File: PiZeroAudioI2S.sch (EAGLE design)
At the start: 53 parts, among them CN1 1X4-BIG, CON1 RPI-ZERO, J1 1X2-3.5MM, U3 NC7WZ16, U4 TPA3144D2PWPR

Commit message: Added I2C and Amplifier
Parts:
- removed C1, C11, C2, C26, C4, C5: 100nF, adafruit:C-USC0805
- removed C10, C15, C16, C20, C22, C25: 1nF, resistor:C-EUC0805
- removed C12: 100uF, adafruit:C-USC0805
- removed C13, C17, C18, C23: 220nF, resistor:C-EUC0805
- removed C14, C19, C21, C24: 1uF, resistor:C-EUC0805
- removed C27: 100UF, adafruit:C-USC0805
- removed CON1: RPI-ZERO, RPI-Zero:RPI-ZERO
- removed L1, L2, L3, L4: BLM31A, HappyBrackets:BLM31A
- removed R10: 39K, adafruit:R-US_R0805
- removed R11: 56K, adafruit:R-US_R0805
- removed R12, R13, R14: 33K, adafruit:R-US_R0805
- removed R15: 10R, adafruit:R-US_R0805
- removed R3, R6: 220, adafruit:R-US_R0805
- removed R4: 100, adafruit:R-US_R0805
- removed R5: 1K8, adafruit:R-US_R0805
- removed R9: 10K, adafruit:R-US_R0805
- removed U1: (no value), adafruit:TXB0104PWR
- removed U3: NC7WZ16, fairchild:NC7WZ16
- removed U4: TPA3144D2PWPR, HappyBrackets:TPA3144D2PWPR
- added U$1: RPI-ZERO, RPI-Zero:RPI-ZERO
- added U$2: (no value), HappyBrackets:LSM6DS33LGA-16-3X3
- added U$3: PCM5100A, HappyBrackets:PCM5100A
- C7: value 47uF -> 100nF; device adafruit:CPOL-US085CS-1AR -> adafruit:C-USC0805
- R1: value 10K -> 220
- R2: value 10K -> 100
- R7: value 100 -> 10K
- R8: value 1K8 -> 10K
- U2: device HappyBrackets:LSM6DS33LGA-16-3X3 -> adafruit:TXB0104PWR
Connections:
- removed net /MUTE: R9.1
- removed net AUDIO-R: C7.-, R8.2, U4.RINP-12
- removed net N$10: C23.2, U4.17-BSPR
- removed net N$11: C16.2, CN1.2, L2.2
- removed net N$12: C15.1, CN1.1, L1.2
- removed net N$13: C18.2, U4.21-BSNR
- removed net N$14: C20.1, CN1.3, L3.2
- removed net N$15: C22.2, CN1.4, L4.2
- removed net N$16: C17.2, U4.22-BSNL
- removed net N$17: C13.2, U4.26-BSPL
- removed net N$18: C13.1, L1.1, U4.25-OUTPL
- removed net N$19: C17.1, L2.1, U4.23-OUTNL
- removed net N$2: R3.2, U3.Y1
- removed net N$20: C18.1, L3.1, U4.20-OUTNR
- removed net N$21: C23.1, L4.1, U4.18-OUTPR
- removed net N$23: R12.1, R13.2, U4.GAIN-6
- removed net N$24: R13.1, R14.2, U4.SSCTRL-7
- removed net N$25: R10.1, R11.2, U4.LIMTHRES-8
- removed net N$26: C19.1, R11.1, R14.1, U4.GVDD-9, U4.LIMRATE-5
- removed net N$3: R6.2, U3.Y2
- removed net N$4: C7.+, C9.1, R6.1, R7.2
- removed net N$5: R9.2, U4./FAULT-2, U4./SD-1
- removed net N$6: U4.LINP-3
- removed net N$7: C14.1, U4.LINN-4
- removed net N$8: C21.1, U4.RINN-11
- removed net N$9: C24.1, R15.1, U4.AVCC-14
- new net OUTL+: CN1.2
- new net OUTL-: CN1.1
- new net OUTR+: CN1.3
- new net OUTR-: CN1.4
- net +3V3: now also C7.1, R7.1, R8.1, U$1.3V3@1, U$2.CS, U$2.SDO, U$2.VDD, U$2.VDDIO, U2.VCCA; no longer C1.1, C5.1, CON1.3V3@1, R1.1, R2.1, U1.VCCA, U2.CS, U2.SDO, U2.VDD, U2.VDDIO, U3.VCC
- net +5V: now also C9.1, U$1.5V0@1, U$1.5V0@2, U2.VCCB; no longer C10.1, C11.1, C12.1, C2.1, C25.1, C26.1, C27.1, CON1.5V0@1, CON1.5V0@2, R15.2, U1.VCCB, U4.15-PVCC, U4.16-PVCC, U4.27-PVCC, U4.28-PVCC
- net AUDIO-L: no longer R5.2
- net GND: now also C7.2, U$1.GND@1, U$1.GND@2, U$1.GND@3, U$1.GND@4, U$1.GND@5, U$1.GND@6, U$1.GND@7, U$1.GND@8, U$2.GND, U$2.GND2, U$2.RES1, U$2.RES2, U$2.RES3, U$2.RES4, U$2.RES5; no longer C1.2, C10.2, C11.2, C12.2, C14.2, C15.2, C16.1, C19.2, C2.2, C20.2, C21.2, C22.1, C24.2, C25.2, C26.2, C27.2, C4.2, C5.2, CON1.GND@1, CON1.GND@2, CON1.GND@3, CON1.GND@4, CON1.GND@5, CON1.GND@6, CON1.GND@7, CON1.GND@8, R10.2, R12.2, R4.1, R5.1, R7.1, R8.1, U1.GND, U2.GND2, U2.RES1, U2.RES2, U2.RES3, U2.RES4, U2.RES5, U3.GND, U4.19-GND, U4.1SPW-13, U4.24-GND, U4.GND-10
- net N$1: now also R1.1; no longer C4.1, R3.1, R4.2
- net PWM-LEFT: now also U$1.GPIO18; no longer CON1.GPIO18, U3.A1
- net PWM-RIGHT: now also U$1.GPIO13; no longer CON1.GPIO13, U3.A2
- net SCL: now also R8.2, U$1.GPIO3/SCL1, U$2.SCL; no longer CON1.GPIO3/SCL1, R2.2, U2.SCL
- net SDA: now also R7.2, U$1.GPIO2/SDA1, U$2.SDA; no longer CON1.GPIO2/SDA1, R1.2, U2.SDA
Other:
- note removed: "Accel + Gyro"
- note removed: "GPIO"
- note removed: "PCM Audio"
- note removed: "PWR amp"
- note removed: "RPI Header"
- note removed: "To Speakers"
- moved on the sheet: C3, C6, C8, C9, CN1, R1, R2, R7, R8

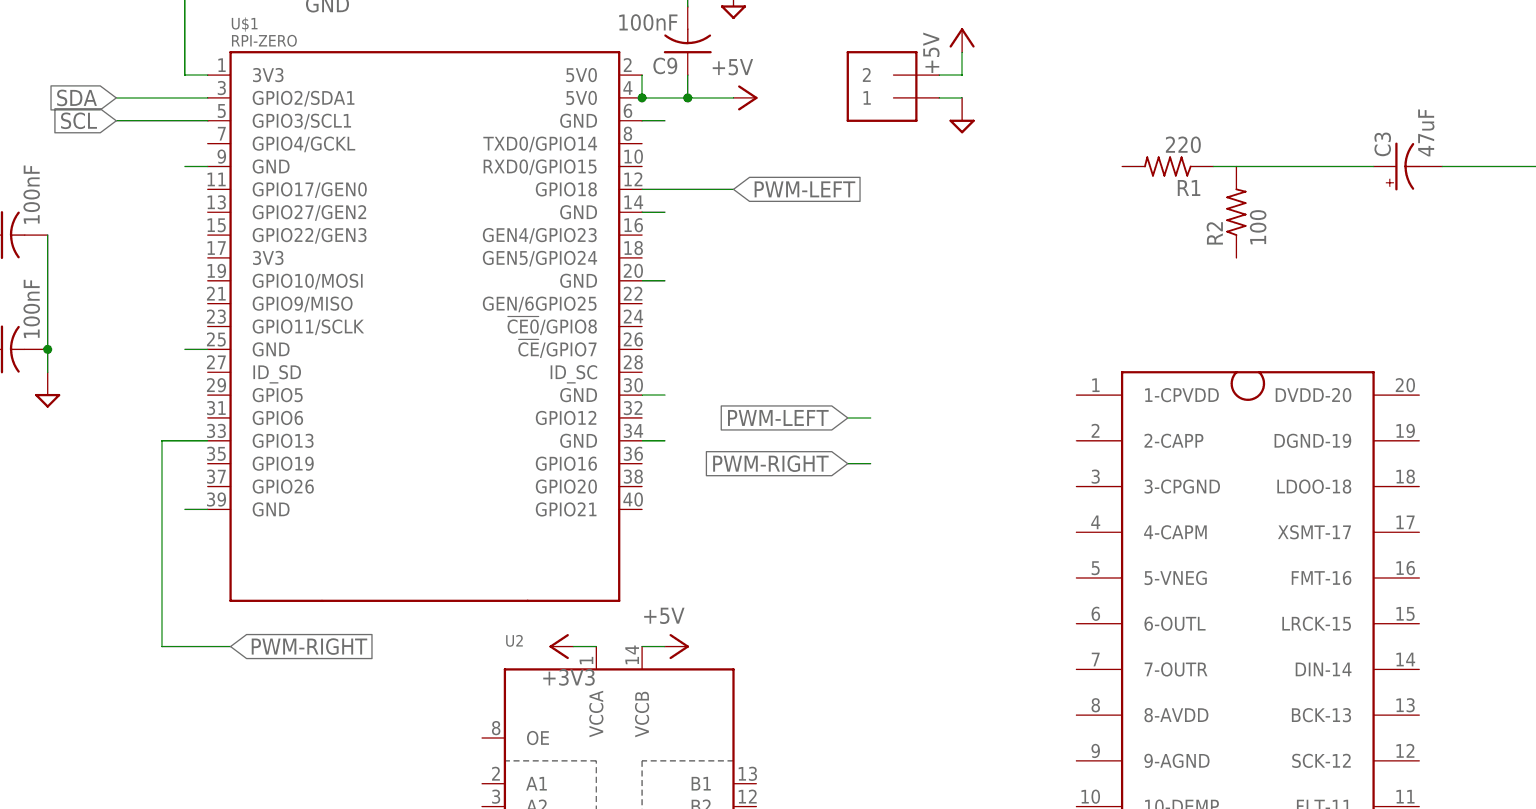
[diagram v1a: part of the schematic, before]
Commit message: Renumbered Pins Placed components for first board
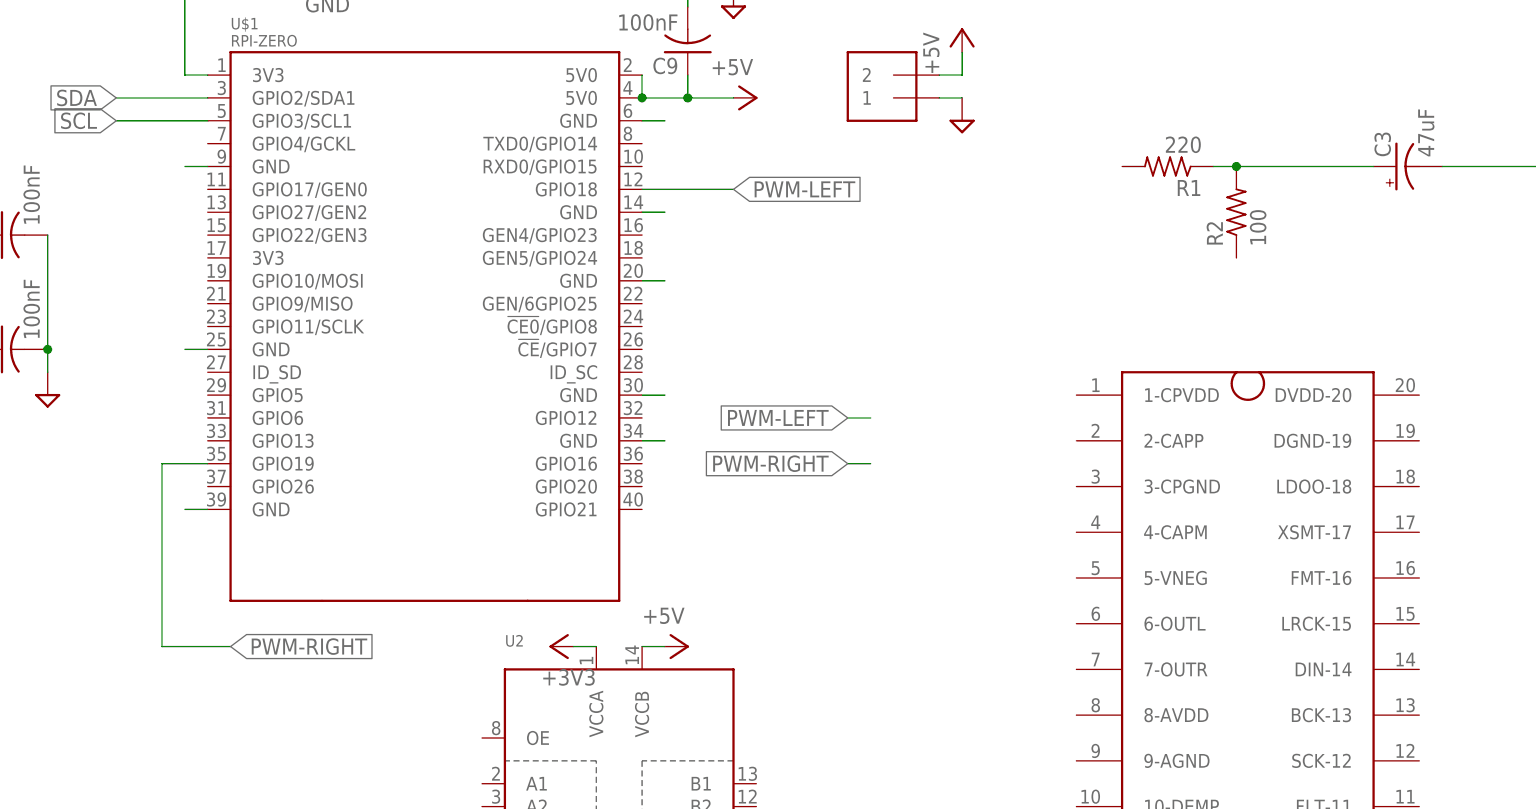
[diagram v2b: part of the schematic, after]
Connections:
- net N$1: now also R2.2
- net PWM-RIGHT: now also U$1.GPIO19; no longer U$1.GPIO13
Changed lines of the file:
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@@
 <net name="PWM-RIGHT" class="0">
 <segment>
-<pinref part="U$1" gate="G$1" pin="GPIO13"/>
-<wire x1="-228.6" y1="88.9" x2="-233.68" y2="88.9" width="0.1524" layer="91"/>
-<wire x1="-233.68" y1="88.9" x2="-233.68" y2="66.04" width="0.1524" layer="91"/>
 <wire x1="-233.68" y1="66.04" x2="-226.06" y2="66.04" width="0.1524" layer="91"/>
 <label x="-226.06" y="66.04" size="1.778" layer="95" xref="yes"/>
+<pinref part="U$1" gate="G$1" pin="GPIO19"/>
+<wire x1="-228.6" y1="86.36" x2="-233.68" y2="86.36" width="0.1524" layer="91"/>
+<wire x1="-233.68" y1="86.36" x2="-233.68" y2="66.04" width="0.1524" layer="91"/>
 </segment>
 <segment>
@@
 <segment>
 <pinref part="R1" gate="G$1" pin="1"/>
-<wire x1="-116.84" y1="119.38" x2="-99.06" y2="119.38" width="0.1524" layer="91"/>
+<wire x1="-116.84" y1="119.38" x2="-114.3" y2="119.38" width="0.1524" layer="91"/>
 <pinref part="C3" gate="G$1" pin="+"/>
+<pinref part="R2" gate="G$1" pin="2"/>
+<wire x1="-114.3" y1="119.38" x2="-99.06" y2="119.38" width="0.1524" layer="91"/>
+<junction x="-114.3" y="119.38"/>
 </segment>
 </net>

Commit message: Pre- grove connector
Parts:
- removed C3: 47uF, adafruit:CPOL-US085CS-1AR
- removed C6, C7, C8: 100nF, adafruit:C-USC0805
- removed R7, R8: 10K, adafruit:R-US_R0805
- removed U$1: RPI-ZERO, RPI-Zero:RPI-ZERO
- removed U$2: (no value), HappyBrackets:LSM6DS33LGA-16-3X3
- removed U$3: PCM5100A, HappyBrackets:PCM5100A
- added C1, C10, C2, C25, C5: 100nF, rcl:C-EUC0603
- added C11: 100uF, adafruit:CPOL-USCT3528
- added C12, C16, C17, C22: 220nF, rcl:C-EUC0603
- added C13, C18, C20, C23: 1uF, rcl:C-EUC0603
- added C14, C15, C19, C21, C24: 1nF, rcl:C-EUC0603
- added C26: 100UF, adafruit:CPOL-USCT3528
- added CON1: RPI-ZERO, RPI-Zero:RPI-ZERO
- added JP1: GPIO, adafruit:PINHD-2X4
- added JP2: (no value), adafruit:PINHD-1X3
- added L1, L2, L3, L4: FB, HappyBrackets:NFZ2MSML0806
- added LED1: (no value), adafruit:LEDCHIP-LED0805
- added Q1: DMG2305UX, HappyBrackets:DMG2305UX
- added R10: 39K, adafruit:R-US_R0603
- added R11: 56K, adafruit:R-US_R0603
- added R12, R13, R14: 33K, adafruit:R-US_R0603
- added R15: 10R, adafruit:R-US_R0603
- added R16, R17: 220, adafruit:R-US_R0603
- added R3: 47K, adafruit:R-US_R0603
- added R4, R9: 10K, adafruit:R-US_R0603
- added SH1, SH2: SHORT, HappyBrackets:SHORT
- added U1: TXB0104PWR, adafruit:TXB0104PWR
- added U3: PCM5101A, HappyBrackets:PCM5101A
- added U4: TPA3144D2PWPR, HappyBrackets:TPA3144D2PWPR
- added U5: DMMT5401, HappyBrackets:DMMT5401
- C9: value 100nF -> 1nF; device adafruit:C-USC0805 -> rcl:C-EUC0603
- R1: value 220 -> 10K; device adafruit:R-US_R0805 -> adafruit:R-US_R0603
- R2: value 100 -> 10K; device adafruit:R-US_R0805 -> adafruit:R-US_R0603
- U2: value (none) -> LSM6DS33; device adafruit:TXB0104PWR -> HappyBrackets:LSM6DS33LGA-16-3X3
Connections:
- removed net AUDIO-L: C3.-
- removed net OUTL+: CN1.2
- removed net OUTL-: CN1.1
- removed net OUTR+: CN1.3
- removed net OUTR-: CN1.4
- removed net PWM-LEFT: U$1.GPIO18
- removed net PWM-RIGHT: U$1.GPIO19
- new net +5V-IN: J1.2, Q1.S, U5G$1.E
- new net /MUTE: CON1.GPIO16, R9.1
- new net ACC-INT1: CON1.GPIO17/GEN0, U2.INT2
- new net ACC-INT2: CON1.GPIO27/GEN2, U2.INT1
- new net AGND: C10.2, C11.-, C13.2, C14.2, C15.1, C18.2, C19.2, C20.2, C21.1, C23.2, C24.2, C25.2, C26.-, C9.2, J1.1, R10.2, R12.2, R3.2, R4.2, SH2.AN, U4.19-GND, U4.1SPW-13, U4.24-GND, U4.GND-10, U4.GND-PAD
- new net AN3V3: SH1.AN
- new net AUDIO-LEFT: U4.LINP-3
- new net AUDIO-RIGHT: U4.RINP-12
- new net GPIO21: CON1.GPIO5, U1.A4
- new net GPIO22: CON1.GPIO6, U1.A3
- new net GPIO23: CON1.GPIO13, U1.A2
- new net GPIO25: CON1.GPIO26, U1.A1
- new net L+: C14.1, CN1.1, L1.2
- new net L-: C15.2, CN1.2, L2.2
- new net N$10: C22.2, U4.17-BSPR
- new net N$11: JP1.1, U1.B1
- new net N$12: JP1.3, U1.B2
- new net N$13: C17.2, U4.21-BSNR
- new net N$14: JP1.5, U1.B3
- new net N$15: JP1.7, U1.B4
- new net N$16: C16.2, U4.22-BSNL
- new net N$17: C12.2, U4.26-BSPL
- new net N$18: C12.1, L1.1, U4.25-OUTPL
- new net N$19: C16.1, L2.1, U4.23-OUTNL
- new net N$2: R4.1, U5G$1.B, U5G$2.B, U5G$2.C
- new net N$20: C17.1, L3.1, U4.20-OUTNR
- new net N$21: C22.1, L4.1, U4.18-OUTPR
- new net N$23: R12.1, R13.2, U4.GAIN-6
- new net N$24: R13.1, R14.2, U4.SSCTRL-7
- new net N$25: R10.1, R11.2, U4.LIMTHRES-8
- new net N$26: C18.1, R11.1, R14.1, U4.GVDD-9, U4.LIMRATE-5
- new net N$5: R9.2, U4./FAULT-2, U4./SD-1
- new net N$6: LED1.C, R16.2
- new net N$7: C13.1, U4.LINN-4
- new net N$8: C20.1, U4.RINN-11
- new net N$9: C23.1, R15.1, U4.AVCC-14
- new net PWM-L: CON1.GPIO19
- new net PWM-R: CON1.GPIO18
- new net PWR-LED: JP2.2, R17.1
- new net R+: C21.2, CN1.4, L4.2
- new net R-: C19.1, CN1.3, L3.2
- net +3V3: now also C1.1, C5.1, CON1.3V3@1, CON1.3V3@2, JP2.1, LED1.A, R1.1, R17.2, R2.1, SH1.DIG, U1.OE, U1.VCCA, U2.CS, U2.SDO, U2.VDD, U2.VDDIO; no longer C6.1, C7.1, C8.1, R7.1, R8.1, U$1.3V3@1, U$2.CS, U$2.SDO, U$2.VDD, U$2.VDDIO, U2.VCCA
- net +5V: now also C10.1, C11.+, C2.1, C24.1, C25.1, C26.+, CON1.5V0@1, CON1.5V0@2, Q1.D, R15.2, U1.VCCB, U4.15-PVCC, U4.16-PVCC, U4.27-PVCC, U4.28-PVCC, U5G$2.E; no longer J1.2, U$1.5V0@1, U$1.5V0@2, U2.VCCB
- net GND: now also C1.2, C2.2, C5.2, CON1.GND@1, CON1.GND@2, CON1.GND@3, CON1.GND@4, CON1.GND@5, CON1.GND@6, CON1.GND@7, CON1.GND@8, JP1.2, JP1.4, JP1.6, JP1.8, JP2.3, R16.1, SH2.DIG, U1.GND, U2.GND2, U2.RES1, U2.RES2, U2.RES3, U2.RES4, U2.RES5; no longer C6.2, C7.2, C8.2, C9.2, J1.1, U$1.GND@1, U$1.GND@2, U$1.GND@3, U$1.GND@4, U$1.GND@5, U$1.GND@6, U$1.GND@7, U$1.GND@8, U$2.GND, U$2.GND2, U$2.RES1, U$2.RES2, U$2.RES3, U$2.RES4, U$2.RES5
- net N$1: now also Q1.G, R3.1, U5G$1.C; no longer C3.+, R1.1, R2.2
- net SCL: now also CON1.GPIO3/SCL1, R2.2, U2.SCL; no longer R8.2, U$1.GPIO3/SCL1, U$2.SCL
- net SDA: now also CON1.GPIO2/SDA1, R1.2, U2.SDA; no longer R7.2, U$1.GPIO2/SDA1, U$2.SDA
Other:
- note added: "Accel + Gyro"
- note added: "GPIO"
- note added: "PWR amp"
- note added: "RPI Header"
- note added: "To Speakers"
- moved on the sheet: C9, CN1, R1, R2
